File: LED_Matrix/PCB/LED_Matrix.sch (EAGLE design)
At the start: 8 parts, among them U1 ATTINY48, U2 ULN2803AFWG

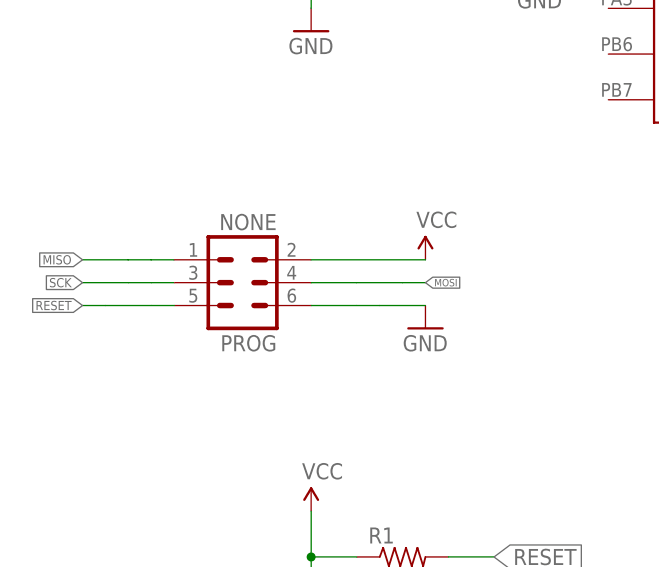
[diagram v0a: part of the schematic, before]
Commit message: led matrix - Moved library parts local.  Added rev and copyright.
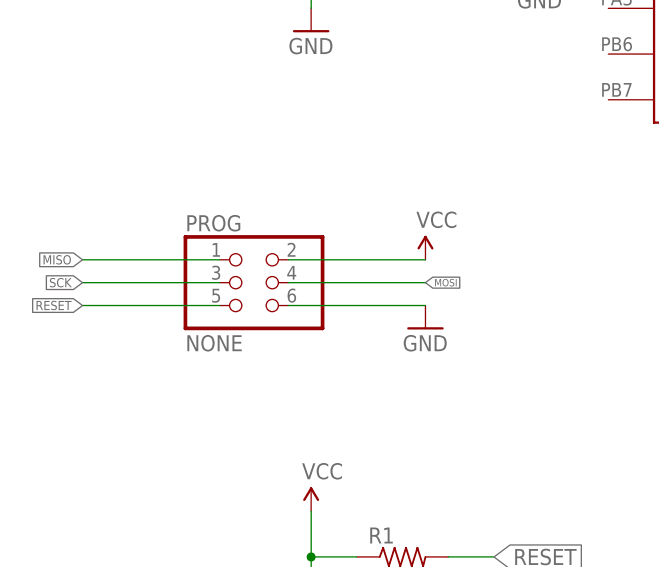
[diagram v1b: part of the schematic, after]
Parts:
- JP1, JP2: device raspberrystem:PINHD-1X6 -> LED_Matrix:PINHD-1X6
- LEDMATRIX: device raspberrystem:8X8_LED_MATRIX -> LED_Matrix:8X8_LED_MATRIX
- PROG: device raspberrystem:MA03-2 -> LED_Matrix:PINHD-2X3
- U1: device raspberrystem:ATTINY48 -> LED_Matrix:ATTINY48
- U2: device raspberrystem:ULN2803AFWG -> LED_Matrix:ULN2803AFWG
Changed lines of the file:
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@@
 <layer number="56" name="wert" color="7" fill="1" visible="no" active="no"/>
 <layer number="57" name="tCAD" color="7" fill="1" visible="no" active="no"/>
+<layer number="90" name="Modules" color="5" fill="1" visible="yes" active="yes"/>
 <layer number="91" name="Nets" color="2" fill="1" visible="yes" active="yes"/>
 <layer number="92" name="Busses" color="1" fill="1" visible="yes" active="yes"/>
@@
 </classes>
 <parts>
-<part name="U1" library="raspberrystem" deviceset="ATTINY48" device=""/>
-<part name="U2" library="raspberrystem" deviceset="ULN2803AFWG" device=""/>
-<part name="LEDMATRIX" library="raspberrystem" deviceset="8X8_LED_MATRIX" device=""/>
+<part name="U1" library="LED_Matrix" deviceset="ATTINY48" device=""/>
+<part name="U2" library="LED_Matrix" deviceset="ULN2803AFWG" device=""/>
+<part name="LEDMATRIX" library="LED_Matrix" deviceset="8X8_LED_MATRIX" device=""/>
 <part name="SUPPLY1" library="SparkFun-Aesthetics" deviceset="VCC" device=""/>
 <part name="SUPPLY2" library="SparkFun-Aesthetics" deviceset="VCC" device=""/>
@@
 <part name="GND3" library="SparkFun-Aesthetics" deviceset="GND" device=""/>
 <part name="FRAME1" library="frames" deviceset="LETTER_L" device=""/>
-<part name="PROG" library="raspberrystem" deviceset="MA03-2" device="" value="NONE"/>
-<part name="JP1" library="raspberrystem" deviceset="PINHD-1X6" device="" value="NONE"/>
-<part name="JP2" library="raspberrystem" deviceset="PINHD-1X6" device="" value="NONE"/>
+<part name="PROG" library="LED_Matrix" deviceset="PINHD-2X3" device="" value="NONE"/>
+<part name="JP1" library="LED_Matrix" deviceset="PINHD-1X6" device="" value="NONE"/>
+<part name="JP2" library="LED_Matrix" deviceset="PINHD-1X6" device="" value="NONE"/>
 </parts>
 <sheets>
@@
 <instance part="FRAME1" gate="G$1" x="-78.74" y="101.6"/>
 <instance part="FRAME1" gate="G$2" x="68.58" y="101.6"/>
-<instance part="PROG" gate="1" x="-43.18" y="182.88" rot="R180"/>
+<instance part="PROG" gate="A" x="-43.18" y="182.88"/>
 <instance part="JP1" gate="A" x="-45.72" y="134.62" rot="MR0"/>
 <instance part="JP2" gate="A" x="7.62" y="134.62"/>
@@
 <segment>
 <pinref part="SUPPLY6" gate="G$1" pin="VCC"/>
-<wire x1="-22.86" y1="185.42" x2="-35.56" y2="185.42" width="0.1524" layer="91"/>
-<pinref part="PROG" gate="1" pin="2"/>
+<wire x1="-22.86" y1="185.42" x2="-38.1" y2="185.42" width="0.1524" layer="91"/>
+<pinref part="PROG" gate="A" pin="2"/>
 </segment>
 <segment>
@@
 <segment>
 <pinref part="GND6" gate="1" pin="GND"/>
-<wire x1="-30.48" y1="180.34" x2="-27.94" y2="180.34" width="0.1524" layer="91"/>
-<pinref part="PROG" gate="1" pin="6"/>
-<wire x1="-27.94" y1="180.34" x2="-22.86" y2="180.34" width="0.1524" layer="91"/>
-<wire x1="-35.56" y1="180.34" x2="-30.48" y2="180.34" width="0.1524" layer="91"/>
+<pinref part="PROG" gate="A" pin="6"/>
+<wire x1="-38.1" y1="180.34" x2="-22.86" y2="180.34" width="0.1524" layer="91"/>
 </segment>
 <segment>
@@
 </segment>
 <segment>
-<wire x1="-53.34" y1="182.88" x2="-55.88" y2="182.88" width="0.1524" layer="91"/>
 <label x="-60.96" y="182.88" size="1.016" layer="95" rot="R180" xref="yes"/>
-<pinref part="PROG" gate="1" pin="3"/>
-<wire x1="-55.88" y1="182.88" x2="-60.96" y2="182.88" width="0.1524" layer="91"/>
-<wire x1="-50.8" y1="182.88" x2="-53.34" y2="182.88" width="0.1524" layer="91"/>
+<pinref part="PROG" gate="A" pin="3"/>
+<wire x1="-45.72" y1="182.88" x2="-60.96" y2="182.88" width="0.1524" layer="91"/>
 </segment>
 </net>
@@
 </segment>
 <segment>
-<wire x1="-53.34" y1="185.42" x2="-55.88" y2="185.42" width="0.1524" layer="91"/>
 <label x="-60.96" y="185.42" size="1.016" layer="95" rot="R180" xref="yes"/>
-<pinref part="PROG" gate="1" pin="1"/>
-<wire x1="-55.88" y1="185.42" x2="-60.96" y2="185.42" width="0.1524" layer="91"/>
-<wire x1="-50.8" y1="185.42" x2="-53.34" y2="185.42" width="0.1524" layer="91"/>
+<pinref part="PROG" gate="A" pin="1"/>
+<wire x1="-45.72" y1="185.42" x2="-60.96" y2="185.42" width="0.1524" layer="91"/>
 </segment>
 </net>
@@
 </segment>
 <segment>
-<wire x1="-30.48" y1="182.88" x2="-25.4" y2="182.88" width="0.1524" layer="91"/>
 <label x="-22.86" y="182.88" size="0.8128" layer="95" xref="yes"/>
-<pinref part="PROG" gate="1" pin="4"/>
-<wire x1="-25.4" y1="182.88" x2="-22.86" y2="182.88" width="0.1524" layer="91"/>
-<wire x1="-35.56" y1="182.88" x2="-30.48" y2="182.88" width="0.1524" layer="91"/>
+<pinref part="PROG" gate="A" pin="4"/>
+<wire x1="-38.1" y1="182.88" x2="-22.86" y2="182.88" width="0.1524" layer="91"/>
 </segment>
 <segment>
@@
 </segment>
 <segment>
-<wire x1="-53.34" y1="180.34" x2="-58.42" y2="180.34" width="0.1524" layer="91"/>
 <label x="-60.96" y="180.34" size="1.016" layer="95" rot="R180" xref="yes"/>
-<pinref part="PROG" gate="1" pin="5"/>
-<wire x1="-58.42" y1="180.34" x2="-60.96" y2="180.34" width="0.1524" layer="91"/>
-<wire x1="-50.8" y1="180.34" x2="-53.34" y2="180.34" width="0.1524" layer="91"/>
-</segment>
-</net>
+<pinref part="PROG" gate="A" pin="5"/>
+<wire x1="-45.72" y1="180.34" x2="-60.96" y2="180.34" width="0.1524" layer="91"/>
+</segment>
+</net>

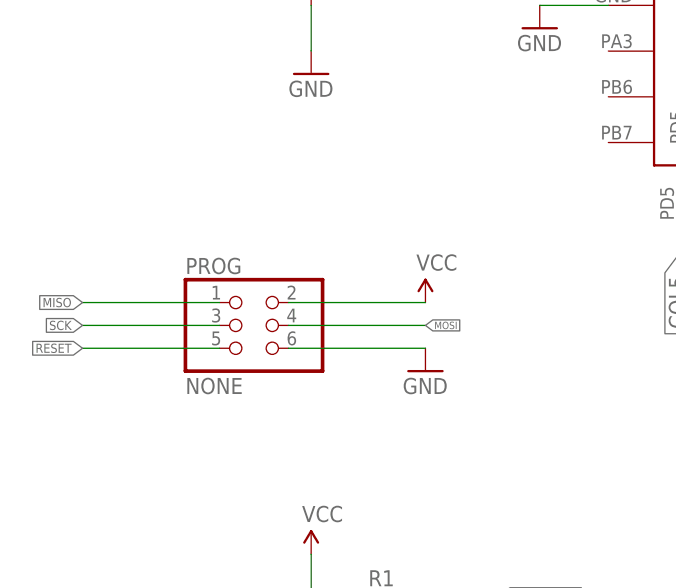
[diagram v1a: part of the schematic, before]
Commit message: led matrix - fixed silkscreen and flipped prog header
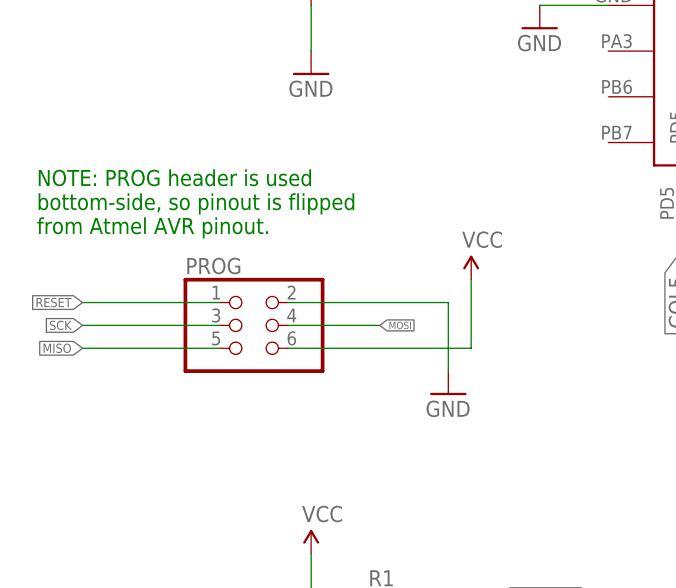
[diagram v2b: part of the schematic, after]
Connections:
- net GND: now also PROG.2; no longer PROG.6
- net MISO: now also PROG.5; no longer PROG.1
- net RESET: now also PROG.1; no longer PROG.5
- net VCC: now also PROG.6; no longer PROG.2
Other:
- note added: "NOTE: PROG header is used bottom-side, so pinout is flipped from Atmel AVR pinout."
